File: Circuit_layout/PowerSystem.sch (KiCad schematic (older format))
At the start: 19 parts, among them U13 PDQ10-D, U14 PDQ15-D, U18 PDQ6-D

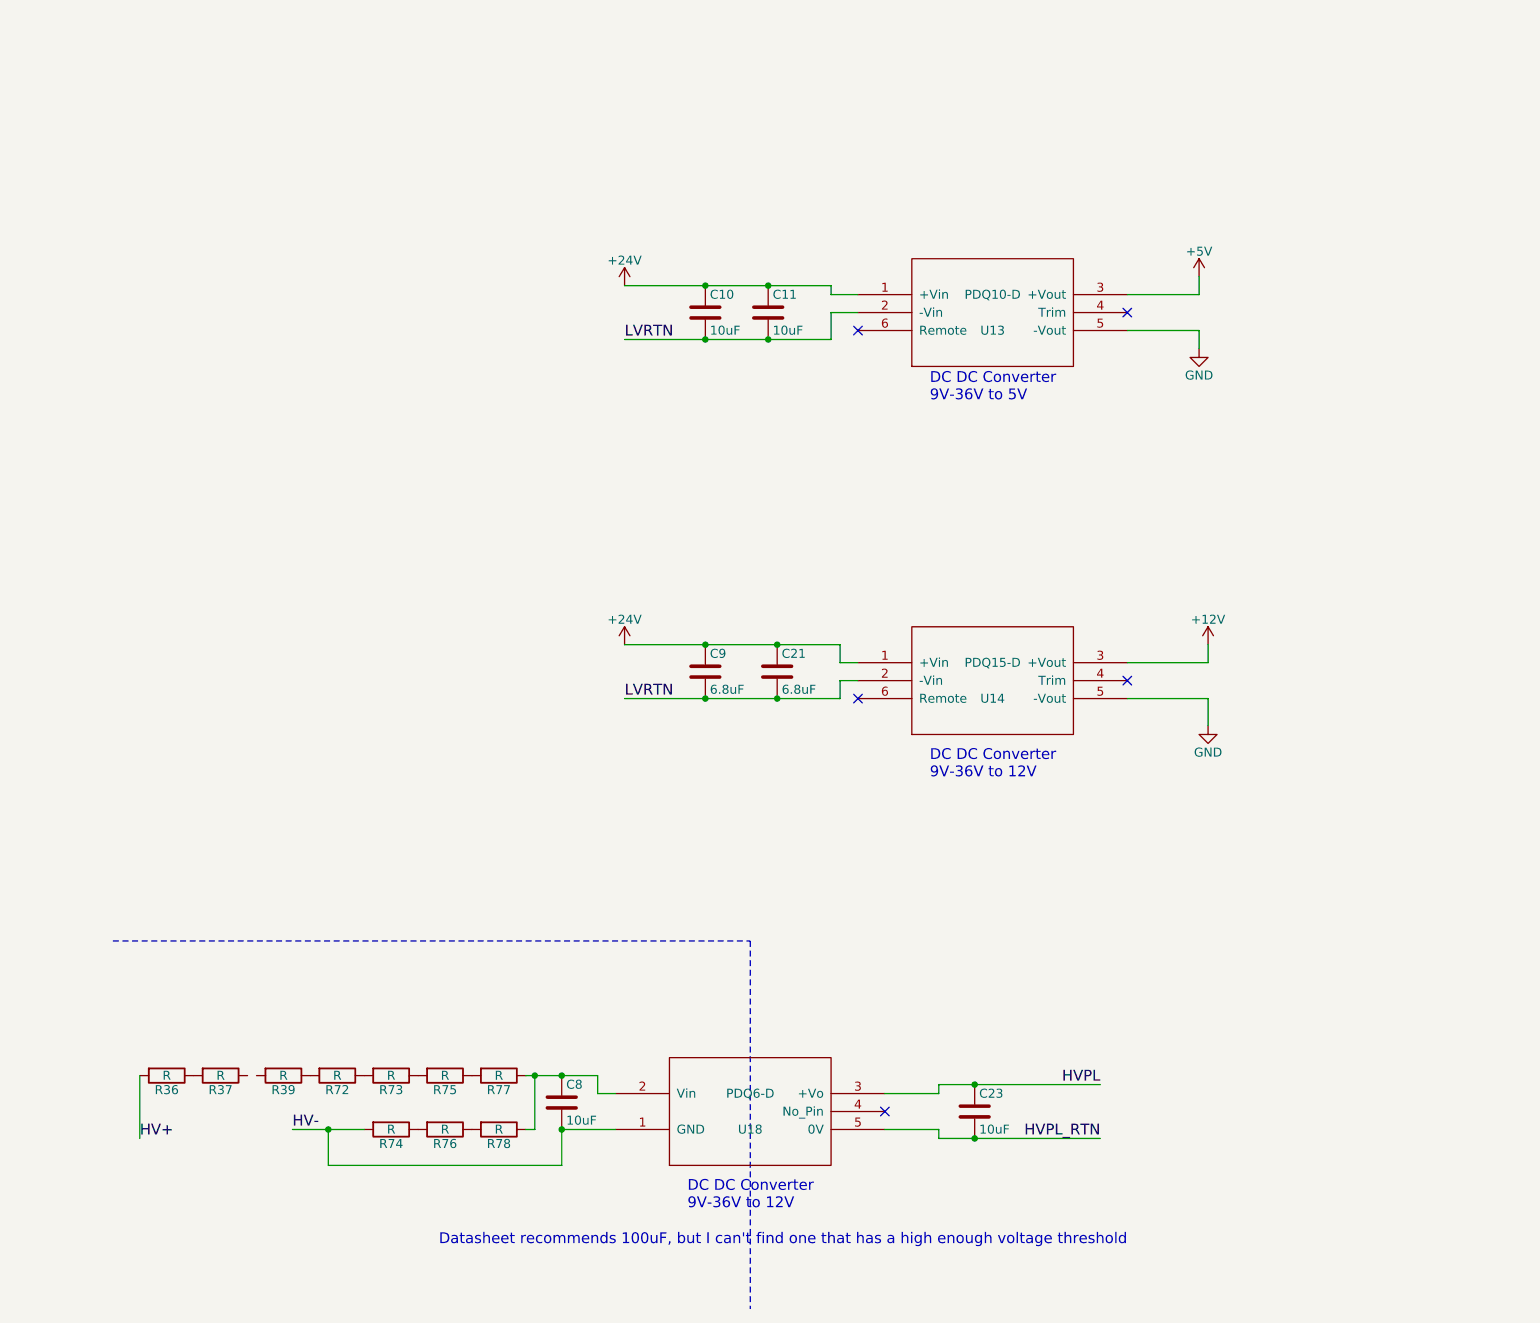
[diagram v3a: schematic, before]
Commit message: got rid of some warnings with nets.
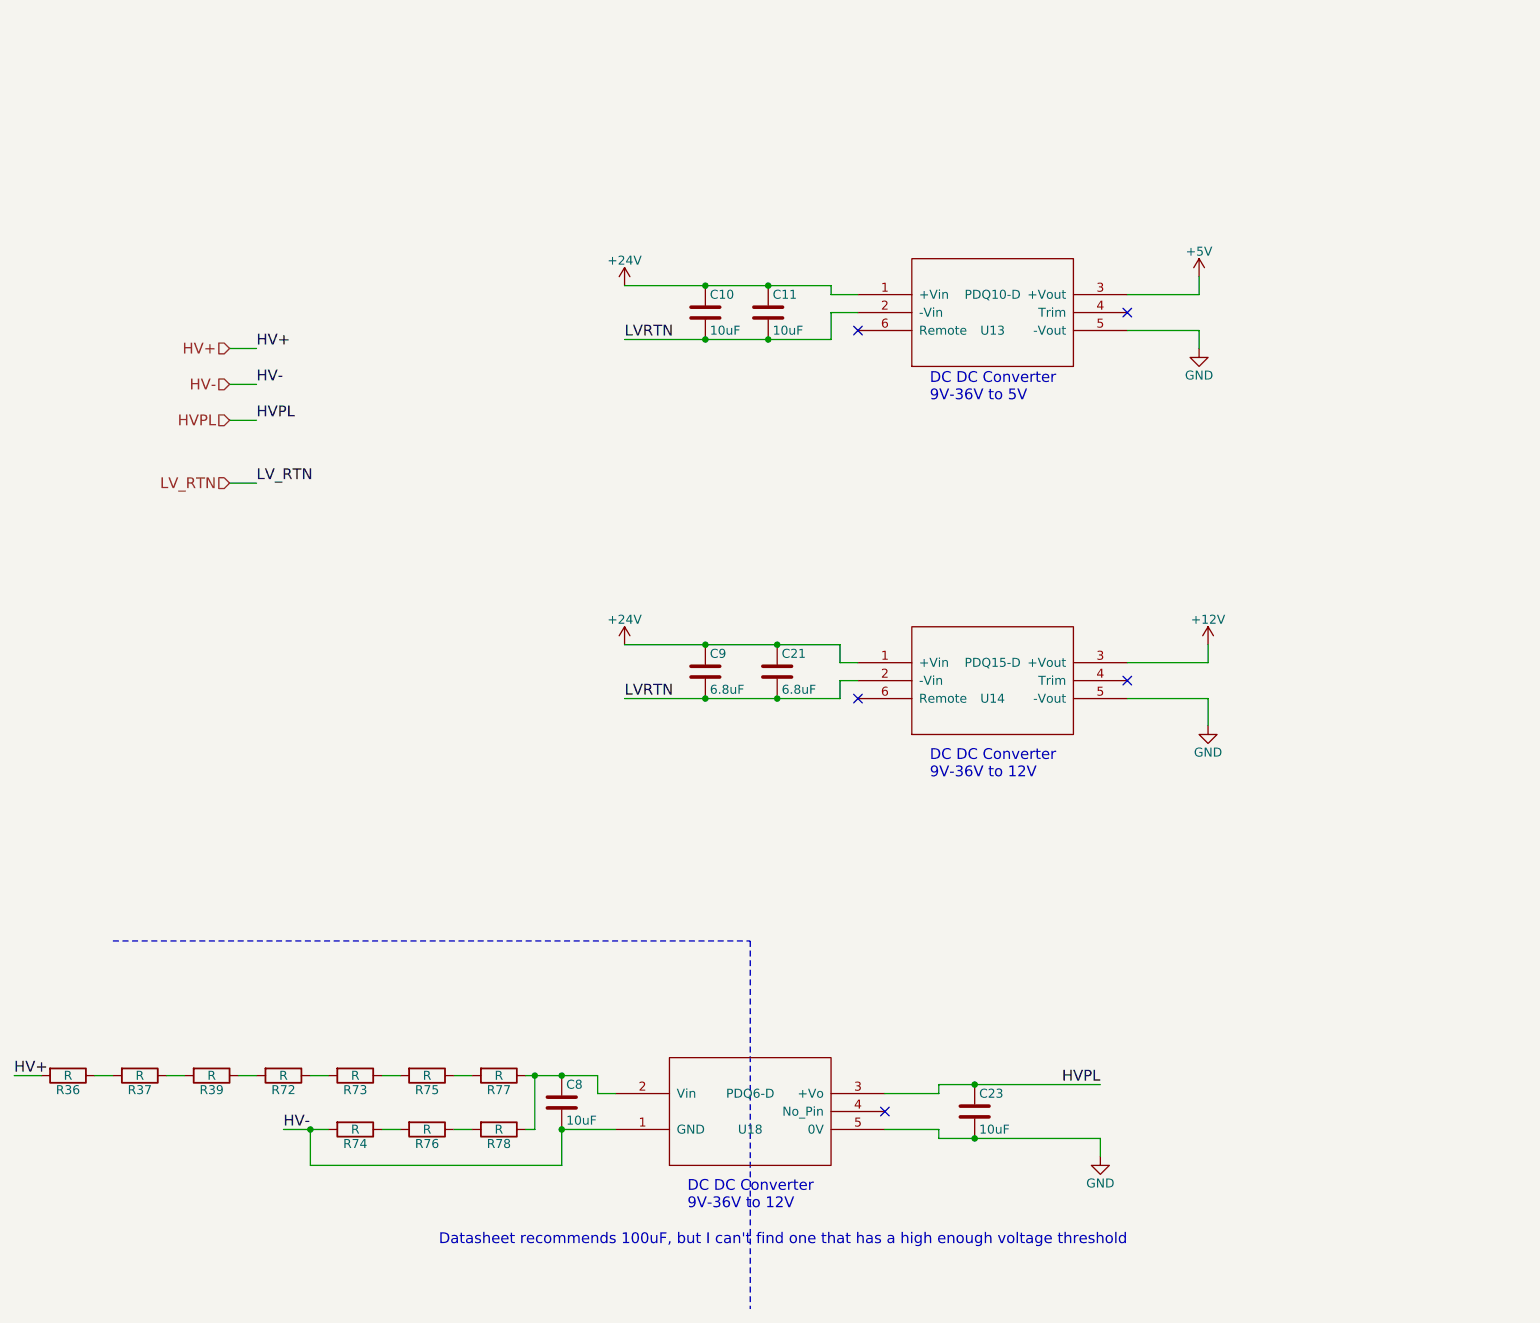
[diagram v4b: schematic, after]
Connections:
- net HVPL_RTN is gone; now on net GND: C23.2, U18.5 (0V)
- net at R37.1: now also R39.2
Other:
- moved on the sheet: R36, R37, R39, R72, R73, R74, R75, R76
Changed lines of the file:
@@
 Connection ~ 3800 2100
 $Comp
-L +24V #PWR036
+L +24V #PWR038
 U 1 1 58AF1DB3
 P 3350 4100
-F 0 "#PWR036" H 3350 3950 50  0001 C CNN
+F 0 "#PWR038" H 3350 3950 50  0001 C CNN
 F 1 "+24V" H 3350 4240 50  0000 C CNN
 F 2 "" H 3350 4100 50  0000 C CNN
@@
 $EndComp
 $Comp
-L +24V #PWR037
+L +24V #PWR039
 U 1 1 58AF1DD3
 P 3350 2100
-F 0 "#PWR037" H 3350 1950 50  0001 C CNN
+F 0 "#PWR039" H 3350 1950 50  0001 C CNN
 F 1 "+24V" H 3350 2240 50  0000 C CNN
 F 2 "" H 3350 2100 50  0000 C CNN
@@
 	6550 2150 6550 2050
 $Comp
-L +5V #PWR038
+L +5V #PWR040
 U 1 1 58AF2067
 P 6550 2050
-F 0 "#PWR038" H 6550 1900 50  0001 C CNN
+F 0 "#PWR040" H 6550 1900 50  0001 C CNN
 F 1 "+5V" H 6550 2190 50  0000 C CNN
 F 2 "" H 6550 2050 50  0000 C CNN
@@
 $EndComp
 $Comp
-L +12V #PWR039
+L +12V #PWR041
 U 1 1 58AF208D
 P 6600 4100
-F 0 "#PWR039" H 6600 3950 50  0001 C CNN
+F 0 "#PWR041" H 6600 3950 50  0001 C CNN
 F 1 "+12V" H 6600 4240 50  0000 C CNN
 F 2 "" H 6600 4100 50  0000 C CNN
@@
 	6550 2350 6550 2450
 $Comp
-L GND #PWR040
+L GND #PWR042
 U 1 1 58AF2561
 P 6550 2450
-F 0 "#PWR040" H 6550 2200 50  0001 C CNN
+F 0 "#PWR042" H 6550 2200 50  0001 C CNN
 F 1 "GND" H 6550 2300 50  0000 C CNN
 F 2 "" H 6550 2450 50  0000 C CNN
@@
 	6600 4400 6600 4550
 $Comp
-L GND #PWR041
+L GND #PWR043
 U 1 1 58AF25AA
 P 6600 4550
-F 0 "#PWR041" H 6600 4300 50  0001 C CNN
+F 0 "#PWR043" H 6600 4300 50  0001 C CNN
 F 1 "GND" H 6600 4400 50  0000 C CNN
 F 2 "" H 6600 4550 50  0000 C CNN
@@
 L R R37
 U 1 1 58B4D9F5
-P 1100 6500
-F 0 "R37" V 1180 6500 50  0000 C CNN
-F 1 "R" V 1100 6500 50  0000 C CNN
-F 2 "" V 1030 6500 50  0000 C CNN
-F 3 "" H 1100 6500 50  0000 C CNN
-	1    1100 6500
+P 650 6500
+F 0 "R37" V 730 6500 50  0000 C CNN
+F 1 "R" V 650 6500 50  0000 C CNN
+F 2 "" V 580 6500 50  0000 C CNN
+F 3 "" H 650 6500 50  0000 C CNN
+	1    650  6500
 	0    1    1    0
 $EndComp
@@
 L R R39
 U 1 1 58B4DA62
+P 1050 6500
+F 0 "R39" V 1130 6500 50  0000 C CNN
+F 1 "R" V 1050 6500 50  0000 C CNN
+F 2 "" V 980 6500 50  0000 C CNN
+F 3 "" H 1050 6500 50  0000 C CNN
+	1    1050 6500
+	0    1    1    0
+$EndComp
+$Comp
+L R R72
+U 1 1 58B4DA9B
 P 1450 6500
-F 0 "R39" V 1530 6500 50  0000 C CNN
+F 0 "R72" V 1530 6500 50  0000 C CNN
 F 1 "R" V 1450 6500 50  0000 C CNN
 F 2 "" V 1380 6500 50  0000 C CNN
@@
 $EndComp
 $Comp
-L R R72
-U 1 1 58B4DA9B
-P 1750 6500
-F 0 "R72" V 1830 6500 50  0000 C CNN
-F 1 "R" V 1750 6500 50  0000 C CNN
-F 2 "" V 1680 6500 50  0000 C CNN
-F 3 "" H 1750 6500 50  0000 C CNN
-	1    1750 6500
-	0    1    1    0
-$EndComp
-$Comp
 L R R73
 U 1 1 58B4DAE3
-P 2050 6500
-F 0 "R73" V 2130 6500 50  0000 C CNN
-F 1 "R" V 2050 6500 50  0000 C CNN
-F 2 "" V 1980 6500 50  0000 C CNN
-F 3 "" H 2050 6500 50  0000 C CNN
-	1    2050 6500
+P 1850 6500
+F 0 "R73" V 1930 6500 50  0000 C CNN
+F 1 "R" V 1850 6500 50  0000 C CNN
+F 2 "" V 1780 6500 50  0000 C CNN
+F 3 "" H 1850 6500 50  0000 C CNN
+	1    1850 6500
 	0    1    1    0
 $EndComp
@@
 L R R75
 U 1 1 58B4DB4B
-P 2350 6500
-F 0 "R75" V 2430 6500 50  0000 C CNN
-F 1 "R" V 2350 6500 50  0000 C CNN
-F 2 "" V 2280 6500 50  0000 C CNN
-F 3 "" H 2350 6500 50  0000 C CNN
-	1    2350 6500
+P 2250 6500
+F 0 "R75" V 2330 6500 50  0000 C CNN
+F 1 "R" V 2250 6500 50  0000 C CNN
+F 2 "" V 2180 6500 50  0000 C CNN
+F 3 "" H 2250 6500 50  0000 C CNN
+	1    2250 6500
 	0    1    1    0
 $EndComp
@@
 L R R36
 U 1 1 58B4DB95
-P 800 6500
-F 0 "R36" V 880 6500 50  0000 C CNN
-F 1 "R" V 800 6500 50  0000 C CNN
-F 2 "" V 730 6500 50  0000 C CNN
-F 3 "" H 800 6500 50  0000 C CNN
-	1    800  6500
+P 250 6500
+F 0 "R36" V 330 6500 50  0000 C CNN
+F 1 "R" V 250 6500 50  0000 C CNN
+F 2 "" V 180 6500 50  0000 C CNN
+F 3 "" H 250 6500 50  0000 C CNN
+	1    250  6500
 	0    1    1    0
 $EndComp
@@
 L R R76
 U 1 1 58B4DD5E
-P 2350 6800
-F 0 "R76" V 2430 6800 50  0000 C CNN
-F 1 "R" V 2350 6800 50  0000 C CNN
-F 2 "" V 2280 6800 50  0000 C CNN
-F 3 "" H 2350 6800 50  0000 C CNN
-	1    2350 6800
+P 2250 6800
+F 0 "R76" V 2330 6800 50  0000 C CNN
+F 1 "R" V 2250 6800 50  0000 C CNN
+F 2 "" V 2180 6800 50  0000 C CNN
+F 3 "" H 2250 6800 50  0000 C CNN
+	1    2250 6800
 	0    1    1    0
 $EndComp
@@
 L R R74
 U 1 1 58B4DDAC
-P 2050 6800
-F 0 "R74" V 2130 6800 50  0000 C CNN
-F 1 "R" V 2050 6800 50  0000 C CNN
-F 2 "" V 1980 6800 50  0000 C CNN
-F 3 "" H 2050 6800 50  0000 C CNN
-	1    2050 6800
-	0    1    1    0
-$EndComp
-Wire Wire Line
-	650  6500 650  6850
-Wire Wire Line
-	1500 6800 1900 6800
-Text Label 1500 6800 0    60   ~ 0
+P 1850 6800
+F 0 "R74" V 1930 6800 50  0000 C CNN
+F 1 "R" V 1850 6800 50  0000 C CNN
+F 2 "" V 1780 6800 50  0000 C CNN
+F 3 "" H 1850 6800 50  0000 C CNN
+	1    1850 6800
+	0    1    1    0
+$EndComp
+Text Label 1450 6800 0    60   ~ 0
 HV-
-Text Label 650  6850 0    60   ~ 0
+Text Label -50  6500 0    60   ~ 0
 HV+
 $Comp
@@
 Text Label 6000 6550 2    60   ~ 0
 HVPL
-Text Label 6000 6850 2    60   ~ 0
-HVPL_RTN
 $Comp
 L C C8
@@
 	3000 6800 3300 6800
 Wire Wire Line
-	3000 6800 3000 7000
-Wire Wire Line
-	3000 7000 1700 7000
-Wire Wire Line
-	1700 7000 1700 6800
-Connection ~ 1700 6800
+	3000 7000 3000 6800
+Wire Wire Line
+	1600 7000 3000 7000
 Wire Wire Line
 	2800 6800 2850 6800
@@
 	2850 6800 2850 6500
 Connection ~ 2850 6500
+Wire Wire Line
+	1450 6800 1700 6800
+Wire Wire Line
+	2000 6800 2100 6800
+Wire Wire Line
+	2400 6800 2500 6800
+Wire Wire Line
+	1600 7000 1600 6800
+Connection ~ 1600 6800
+Wire Wire Line
+	400  6500 500  6500
+Wire Wire Line
+	800  6500 900  6500
+Wire Wire Line
+	1200 6500 1300 6500
+Wire Wire Line
+	1600 6500 1700 6500
+Wire Wire Line
+	2000 6500 2100 6500
+Wire Wire Line
+	2400 6500 2500 6500
+Wire Wire Line
+	100  6500 -50  6500
+Text HLabel 1150 2450 0    60   Input ~ 0
+HV+
+Text HLabel 1150 2650 0    60   Input ~ 0
+HV-
+Text HLabel 1150 2850 0    60   Input ~ 0
+HVPL
+Text HLabel 1150 3200 0    60   Input ~ 0
+LV_RTN
+Wire Wire Line
+	1150 2450 1300 2450
+Wire Wire Line
+	1150 2650 1300 2650
+Wire Wire Line
+	1150 2850 1300 2850
+Wire Wire Line
+	1150 3200 1300 3200
+Text Label 1300 2450 0    60   ~ 0
+HV+
+Text Label 1300 2650 0    60   ~ 0
+HV-
+Text Label 1300 2850 0    60   ~ 0
+HVPL
+Text Label 1300 3200 0    60   ~ 0
+LV_RTN
+$Comp
+L GND #PWR044
+U 1 1 58BA25F0
+P 6000 6950
+F 0 "#PWR044" H 6000 6700 50  0001 C CNN
+F 1 "GND" H 6000 6800 50  0000 C CNN
+F 2 "" H 6000 6950 50  0000 C CNN
+F 3 "" H 6000 6950 50  0000 C CNN
+	1    6000 6950
+	1    0    0    -1
+$EndComp
+Wire Wire Line
+	6000 6850 6000 6950
 $EndSCHEMATC

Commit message: Working on neatining up schematic and working on top level diagram
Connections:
- net LVRTN: no longer C10.2, C11.2, U13.2 (-Vin)
- net LV_RTN: now also C10.2, C11.2, U13.2 (-Vin)
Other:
- note added: "High Voltage"
- moved on the sheet: C10, C11, C21, C23, C8, C9, R36, R37, R39, R72, R73, R74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
